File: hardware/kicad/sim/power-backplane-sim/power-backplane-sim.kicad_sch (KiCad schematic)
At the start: 28 parts, among them P500 P500, P501 P501, P502 P502, P503 P503, P504 P504, P505 P505, P506 P506, P601 P601

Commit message: Board 2 power-backplane: ERC 0, ripple-filter sim -50dB @350kHz verified, routed PCB DRC 0/0, fab outputs; URB->URA2415YMD-10WR3 part correction (URB is single-output)
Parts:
- removed C500: 220u, Capacitor_THT:CP_Radial_D10.0mm_P5.00mm, symbol Device:C_Polarized
- removed C507: 47u, Capacitor_THT:CP_Radial_D6.3mm_P2.50mm, symbol Device:C_Polarized
- removed C508: 100n, Capacitor_SMD:C_0805_2012Metric, symbol Device:C
- removed C509: 100u, Capacitor_THT:CP_Radial_D10.0mm_P5.00mm, symbol Device:C_Polarized
- removed C510, C511: 10u, Capacitor_THT:CP_Radial_D6.3mm_P2.50mm, symbol Device:C_Polarized
- removed R500: 0, Resistor_SMD:R_1206_3216Metric, symbol Device:R
- added RL1, RL2: 60, Resistor_SMD:R_0805_2012Metric, symbol Device:R
- added V1, V2: 15V + ripple, symbol Simulation_SPICE:VDC
- added V3: 0V AGND bond, symbol Simulation_SPICE:VDC
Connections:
- net +15VA: now also RL1.1
- net +15VRAW: now also V1.1
- net -15VA: now also RL2.1
- net -15VRAW: now also V2.2
- net AGND: now also RL1.2, RL2.2, V3.1
- new net GND: V1.2, V2.1, V3.2
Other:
- note added: ".ac dec 50 100 10Meg ; plots rail ripple rejection: probe v(+15va), v(-15va) ; the bead+LC filter should be >40 dB down at the module's ; 350 kHz switching frequency"
- note added: "SIM: DC-DC MODULE MODELED AS 15V SOURCES WITH 1V AC RIPPLE"
- title: GAS Rev A - Power Backplane Board -> GAS Rev A - Power Backplane - SIMULATION TESTBENCH

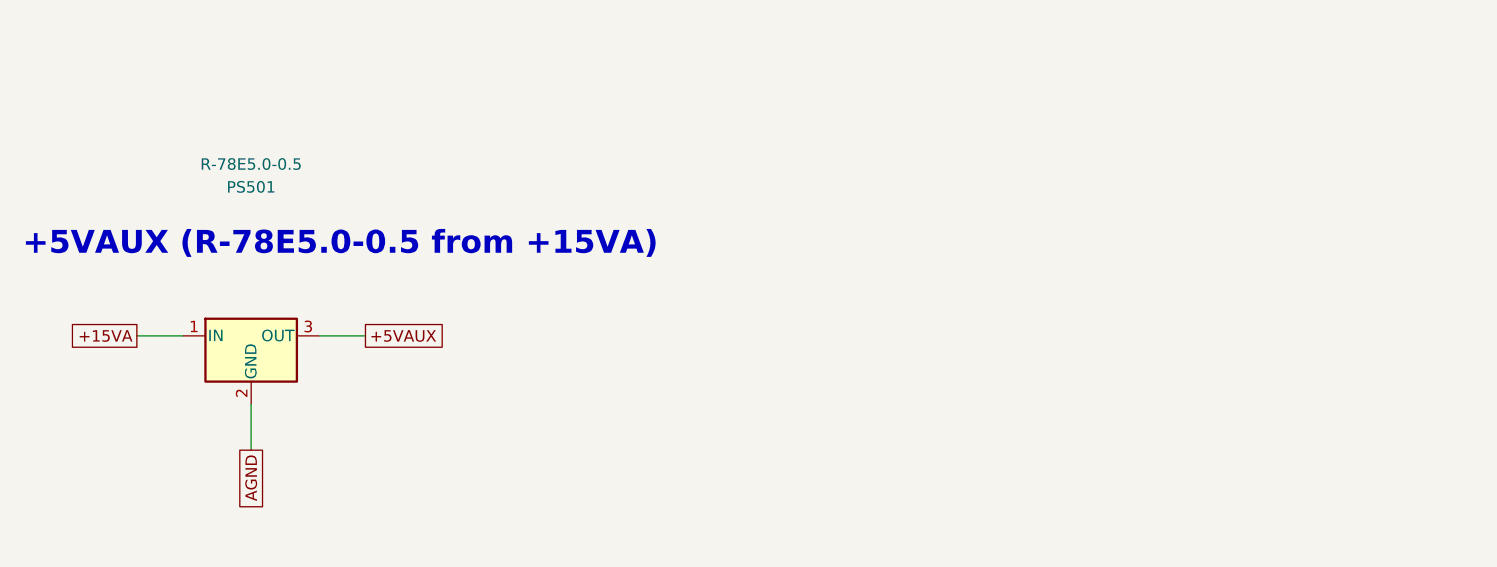
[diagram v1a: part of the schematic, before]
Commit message: Schematic review (kicad-schematic-review skill): F1 R-78E moved to +15VRAW, F2 mono-float bleed R25; both boards re-routed/verified; datasheet cache, per-instance reviews, schematic_review.md
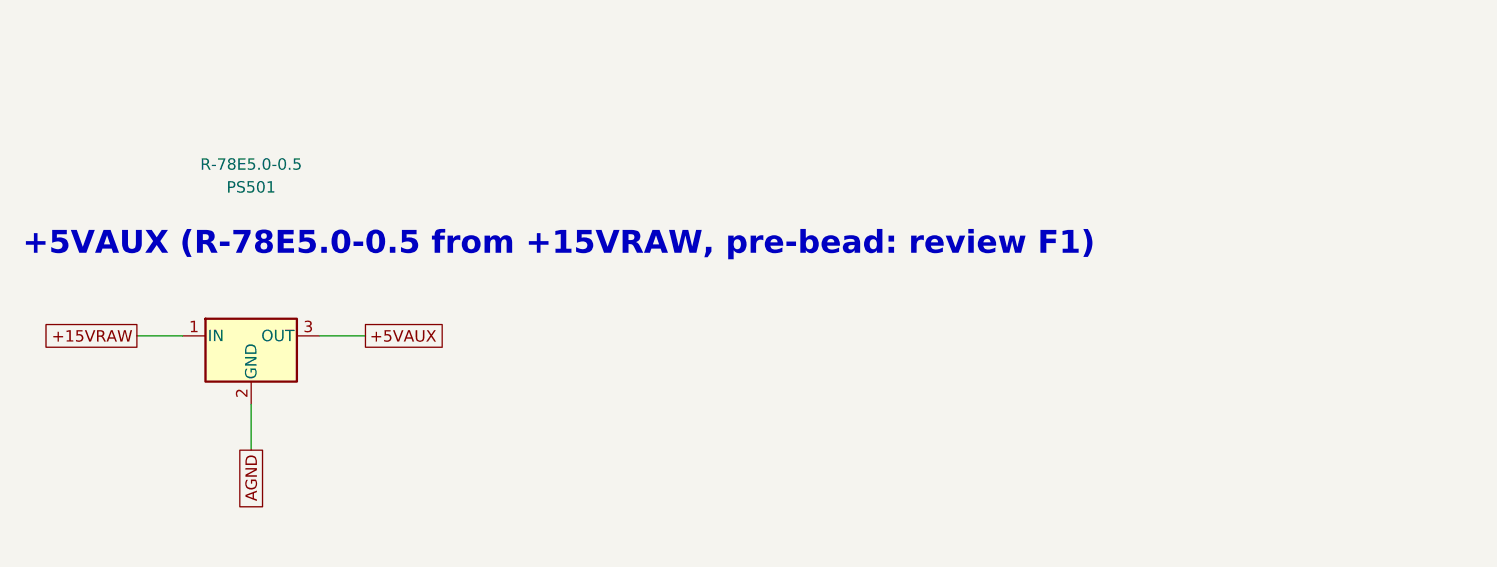
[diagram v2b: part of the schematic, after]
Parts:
- removed FB500: BLM18PG471SN1, Inductor_SMD:L_0603_1608Metric, symbol Device:FerriteBead
- removed P500: P500, Connector_JST:JST_XH_B2B-XH-A_1x02_P2.50mm_Vertical, symbol Connector_Generic:Conn_01x02
- removed V1: 15V + ripple, symbol Simulation_SPICE:VDC
- added C506: 100n, Capacitor_SMD:C_1206_3216Metric, symbol Device:C
- added RL2: 60, Resistor_SMD:R_0805_2012Metric, symbol Device:R
- added TVS500: SMAJ33A, Diode_SMD:D_SMA, symbol Device:D_TVS
- C501: renamed from C502; value 10u -> 100u; footprint Capacitor_SMD:C_1206_3216Metric -> Capacitor_THT:CP_Radial_D6.3mm_P2.50mm; symbol Device:C -> Device:C_Polarized; Voltage (none) -> 25V
- C502: renamed from C503; value 100n -> 10u
- C503: renamed from FB501; value BLM18PG471SN1 -> 100n; footprint Inductor_SMD:L_0603_1608Metric -> Capacitor_SMD:C_1206_3216Metric; symbol Device:FerriteBead -> Device:C
- C504: renamed from C505; value 10u -> 100u; footprint Capacitor_SMD:C_1206_3216Metric -> Capacitor_THT:CP_Radial_D6.3mm_P2.50mm; symbol Device:C -> Device:C_Polarized; Voltage (none) -> 25V
- C505: renamed from C506; value 100n -> 10u
- D500: renamed from F500; value 1.1A PTC MF-MSMF110 -> SS34; footprint Fuse:Fuse_1812_4532Metric -> Diode_SMD:D_SMA; symbol Device:Polyfuse -> Device:D_Schottky
- F500: renamed from TVS500; value SMAJ33A -> 1.1A PTC MF-MSMF110; footprint Diode_SMD:D_SMA -> Fuse:Fuse_1812_4532Metric; symbol Device:D_TVS -> Device:Polyfuse
- FB500: renamed from C501; value 100u -> BLM18PG471SN1; footprint Capacitor_THT:CP_Radial_D6.3mm_P2.50mm -> Inductor_SMD:L_0603_1608Metric; symbol Device:C_Polarized -> Device:FerriteBead; Voltage 25V -> (none)
- FB501: renamed from C504; value 100u -> BLM18PG471SN1; footprint Capacitor_THT:CP_Radial_D6.3mm_P2.50mm -> Inductor_SMD:L_0603_1608Metric; symbol Device:C_Polarized -> Device:FerriteBead; Voltage 25V -> (none)
- P500: renamed from D500; value SS34 -> P500; footprint Diode_SMD:D_SMA -> Connector_JST:JST_XH_B2B-XH-A_1x02_P2.50mm_Vertical; symbol Device:D_Schottky -> Connector_Generic:Conn_01x02
- V2: renamed from V3; value 0V AGND bond -> 15V + ripple
- V3: renamed from RL1; value 60 -> 0V AGND bond; footprint Resistor_SMD:R_0805_2012Metric -> (none); symbol Device:R -> Simulation_SPICE:VDC
- renumbered RL2 to RL1, V2 to V1
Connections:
- net +15VA: now also C503.1, FB500.2, RL1.1; no longer FB500.1, PS501.1 (IN), V3.1
- net +15VRAW: now also FB500.1, PS501.1 (IN), V1.1
- net +30V_D: now also F500.1; no longer P500.1 (K)
- net +30V_F: now also F500.2, TVS500.1 (A1); no longer D500.2, F500.1 (A1)
- net +30V_RAW: now also D500.2 (A), P500.1 (Pin_1); no longer P500.2 (A)
- net -15VA: now also C504.2, C506.1, RL2.1; no longer C503.2, C504.1, RL1.1
- net -15VRAW: now also FB501.1, V2.2; no longer C503.1, V1.2
- net AGND: now also C503.2, C504.1, V3.1, C506.2, RL2.2; no longer C504.2, FB500.2, FB501.1, V2.1, V3.2
- net GND: now also V1.2, V2.1, V3.2; no longer V1.1, V2.2
- net GND_IN: now also P500.2 (Pin_2), TVS500.2 (A2); no longer F500.2 (A2)
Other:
- note added: "+5VAUX (R-78E5.0-0.5 from +15VRAW, pre-bead: review F1)"
- note removed: "+5VAUX (R-78E5.0-0.5 from +15VA)"
- moved on the sheet: C502, C505, D500, F500, RL1, V1, V2
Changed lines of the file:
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@@
 		)
 	)
-	(text "+5VAUX (R-78E5.0-0.5 from +15VA)"
+	(text "+5VAUX (R-78E5.0-0.5 from +15VRAW, pre-bead: review F1)"
 		(exclude_from_sim yes)
 		(at 25.4 289.56 0)
@@
 		)
 	)
-	(global_label "+15VA"
+	(global_label "+15VRAW"
 		(shape passive)
 		(at 38.10 299.72 180)
@@
 		(instances
 			(project "power-backplane-sim"
-				(path "/f0196b2d-ecd5-586f-9fae-c6720a86e92b"
+				(path "/688e4b66-327a-56d5-8053-300f5cf96d9c"
 					(reference "P500")
 					(unit 1)
@@
 		(instances
 			(project "power-backplane-sim"
-				(path "/f0196b2d-ecd5-586f-9fae-c6720a86e92b"
+				(path "/688e4b66-327a-56d5-8053-300f5cf96d9c"
 					(reference "D500")
 					(unit 1)
@@
 		(instances
 			(project "power-backplane-sim"
-				(path "/f0196b2d-ecd5-586f-9fae-c6720a86e92b"
+				(path "/688e4b66-327a-56d5-8053-300f5cf96d9c"
 					(reference "F500")
 					(unit 1)
@@
 		(instances
 			(project "power-backplane-sim"
-				(path "/f0196b2d-ecd5-586f-9fae-c6720a86e92b"
+				(path "/688e4b66-327a-56d5-8053-300f5cf96d9c"
 					(reference "TVS500")
 					(unit 1)
@@
 		(instances
 			(project "power-backplane-sim"
-				(path "/f0196b2d-ecd5-586f-9fae-c6720a86e92b"
+				(path "/688e4b66-327a-56d5-8053-300f5cf96d9c"
 					(reference "PS500")
 					(unit 1)
@@
 		(instances
 			(project "power-backplane-sim"
-				(path "/f0196b2d-ecd5-586f-9fae-c6720a86e92b"
+				(path "/688e4b66-327a-56d5-8053-300f5cf96d9c"
 					(reference "FB500")
 					(unit 1)
@@
 		(instances
 			(project "power-backplane-sim"
-				(path "/f0196b2d-ecd5-586f-9fae-c6720a86e92b"
+				(path "/688e4b66-327a-56d5-8053-300f5cf96d9c"
 					(reference "C501")
 					(unit 1)
@@
 		(instances
 			(project "power-backplane-sim"
-				(path "/f0196b2d-ecd5-586f-9fae-c6720a86e92b"
+				(path "/688e4b66-327a-56d5-8053-300f5cf96d9c"
 					(reference "C502")
 					(unit 1)
@@
 		(instances
 			(project "power-backplane-sim"
-				(path "/f0196b2d-ecd5-586f-9fae-c6720a86e92b"
+				(path "/688e4b66-327a-56d5-8053-300f5cf96d9c"
 					(reference "C503")
 					(unit 1)
@@
 		(instances
 			(project "power-backplane-sim"
-				(path "/f0196b2d-ecd5-586f-9fae-c6720a86e92b"
+				(path "/688e4b66-327a-56d5-8053-300f5cf96d9c"
 					(reference "FB501")
 					(unit 1)
@@
 		(instances
 			(project "power-backplane-sim"
-				(path "/f0196b2d-ecd5-586f-9fae-c6720a86e92b"
+				(path "/688e4b66-327a-56d5-8053-300f5cf96d9c"
 					(reference "C504")
 					(unit 1)
@@
 		(instances
 			(project "power-backplane-sim"
-				(path "/f0196b2d-ecd5-586f-9fae-c6720a86e92b"
+				(path "/688e4b66-327a-56d5-8053-300f5cf96d9c"
 					(reference "C505")
 					(unit 1)
@@
 		(instances
 			(project "power-backplane-sim"
-				(path "/f0196b2d-ecd5-586f-9fae-c6720a86e92b"
+				(path "/688e4b66-327a-56d5-8053-300f5cf96d9c"
 					(reference "C506")
 					(unit 1)
@@
 		(instances
 			(project "power-backplane-sim"
-				(path "/f0196b2d-ecd5-586f-9fae-c6720a86e92b"
+				(path "/688e4b66-327a-56d5-8053-300f5cf96d9c"
 					(reference "PS501")
 					(unit 1)
@@
 		(instances
 			(project "power-backplane-sim"
-				(path "/f0196b2d-ecd5-586f-9fae-c6720a86e92b"
+				(path "/688e4b66-327a-56d5-8053-300f5cf96d9c"
 					(reference "P501")
 					(unit 1)
@@
 		(instances
 			(project "power-backplane-sim"
-				(path "/f0196b2d-ecd5-586f-9fae-c6720a86e92b"
+				(path "/688e4b66-327a-56d5-8053-300f5cf96d9c"
 					(reference "P502")
 					(unit 1)
@@
 		(instances
 			(project "power-backplane-sim"
-				(path "/f0196b2d-ecd5-586f-9fae-c6720a86e92b"
+				(path "/688e4b66-327a-56d5-8053-300f5cf96d9c"
 					(reference "P503")
 					(unit 1)
@@
 		(instances
 			(project "power-backplane-sim"
-				(path "/f0196b2d-ecd5-586f-9fae-c6720a86e92b"
+				(path "/688e4b66-327a-56d5-8053-300f5cf96d9c"
 					(reference "P504")
 					(unit 1)
@@
 		(instances
 			(project "power-backplane-sim"
-				(path "/f0196b2d-ecd5-586f-9fae-c6720a86e92b"
+				(path "/688e4b66-327a-56d5-8053-300f5cf96d9c"
 					(reference "P505")
 					(unit 1)
@@
 		(instances
 			(project "power-backplane-sim"
-				(path "/f0196b2d-ecd5-586f-9fae-c6720a86e92b"
+				(path "/688e4b66-327a-56d5-8053-300f5cf96d9c"
 					(reference "P506")
 					(unit 1)
@@
 		(instances
 			(project "power-backplane-sim"
-				(path "/f0196b2d-ecd5-586f-9fae-c6720a86e92b"
+				(path "/688e4b66-327a-56d5-8053-300f5cf96d9c"
 					(reference "P601")
 					(unit 1)
@@
 		(instances
 			(project "power-backplane-sim"
-				(path "/f0196b2d-ecd5-586f-9fae-c6720a86e92b"
+				(path "/688e4b66-327a-56d5-8053-300f5cf96d9c"
 					(reference "#FLG500")
 					(unit 1)
@@
 		(instances
 			(project "power-backplane-sim"
-				(path "/f0196b2d-ecd5-586f-9fae-c6720a86e92b"
+				(path "/688e4b66-327a-56d5-8053-300f5cf96d9c"
 					(reference "#FLG501")
 					(unit 1)
@@
 		(instances
 			(project "power-backplane-sim"
-				(path "/f0196b2d-ecd5-586f-9fae-c6720a86e92b"
+				(path "/688e4b66-327a-56d5-8053-300f5cf96d9c"
 					(reference "#FLG502")
 					(unit 1)
@@
 		(instances
 			(project "power-backplane-sim"
-				(path "/f0196b2d-ecd5-586f-9fae-c6720a86e92b"
+				(path "/688e4b66-327a-56d5-8053-300f5cf96d9c"
 					(reference "#FLG503")
 					(unit 1)
@@
 		(instances
 			(project "power-backplane-sim"
-				(path "/f0196b2d-ecd5-586f-9fae-c6720a86e92b"
+				(path "/688e4b66-327a-56d5-8053-300f5cf96d9c"
 					(reference "#FLG504")
 					(unit 1)
@@
 		(instances
 			(project "power-backplane-sim"
-				(path "/f0196b2d-ecd5-586f-9fae-c6720a86e92b"
+				(path "/688e4b66-327a-56d5-8053-300f5cf96d9c"
 					(reference "#FLG505")
 					(unit 1)
@@
 		(instances
 			(project "power-backplane-sim"
-				(path "/f0196b2d-ecd5-586f-9fae-c6720a86e92b"
+				(path "/688e4b66-327a-56d5-8053-300f5cf96d9c"
 					(reference "#FLG506")
 					(unit 1)
@@
 		(instances
 			(project "power-backplane-sim"
-				(path "/f0196b2d-ecd5-586f-9fae-c6720a86e92b"
+				(path "/688e4b66-327a-56d5-8053-300f5cf96d9c"
 					(reference "#FLG507")
 					(unit 1)
@@
 		(instances
 			(project "power-backplane-sim"
-				(path "/f0196b2d-ecd5-586f-9fae-c6720a86e92b"
+				(path "/688e4b66-327a-56d5-8053-300f5cf96d9c"
 					(reference "V1")
 					(unit 1)
@@
 		(instances
 			(project "power-backplane-sim"
-				(path "/f0196b2d-ecd5-586f-9fae-c6720a86e92b"
+				(path "/688e4b66-327a-56d5-8053-300f5cf96d9c"
 					(reference "V2")
 					(unit 1)
@@
 		(instances
 			(project "power-backplane-sim"
-				(path "/f0196b2d-ecd5-586f-9fae-c6720a86e92b"
+				(path "/688e4b66-327a-56d5-8053-300f5cf96d9c"
 					(reference "V3")
 					(unit 1)
@@
 		(instances
 			(project "power-backplane-sim"
-				(path "/f0196b2d-ecd5-586f-9fae-c6720a86e92b"
+				(path "/688e4b66-327a-56d5-8053-300f5cf96d9c"
 					(reference "RL1")
 					(unit 1)
@@
 		(instances
 			(project "power-backplane-sim"
-				(path "/f0196b2d-ecd5-586f-9fae-c6720a86e92b"
+				(path "/688e4b66-327a-56d5-8053-300f5cf96d9c"
 					(reference "RL2")
 					(unit 1)
@@
 		(instances
 			(project "power-backplane-sim"
-				(path "/f0196b2d-ecd5-586f-9fae-c6720a86e92b"
+				(path "/688e4b66-327a-56d5-8053-300f5cf96d9c"
 					(reference "#PWR01")
 					(unit 1)
@@
 		(instances
 			(project "power-backplane-sim"
-				(path "/f0196b2d-ecd5-586f-9fae-c6720a86e92b"
+				(path "/688e4b66-327a-56d5-8053-300f5cf96d9c"
 					(reference "#FLG201")
 					(unit 1)
